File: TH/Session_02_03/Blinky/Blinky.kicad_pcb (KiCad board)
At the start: 2 copper layers, 12 parts, among them U1 TLC551CD‎

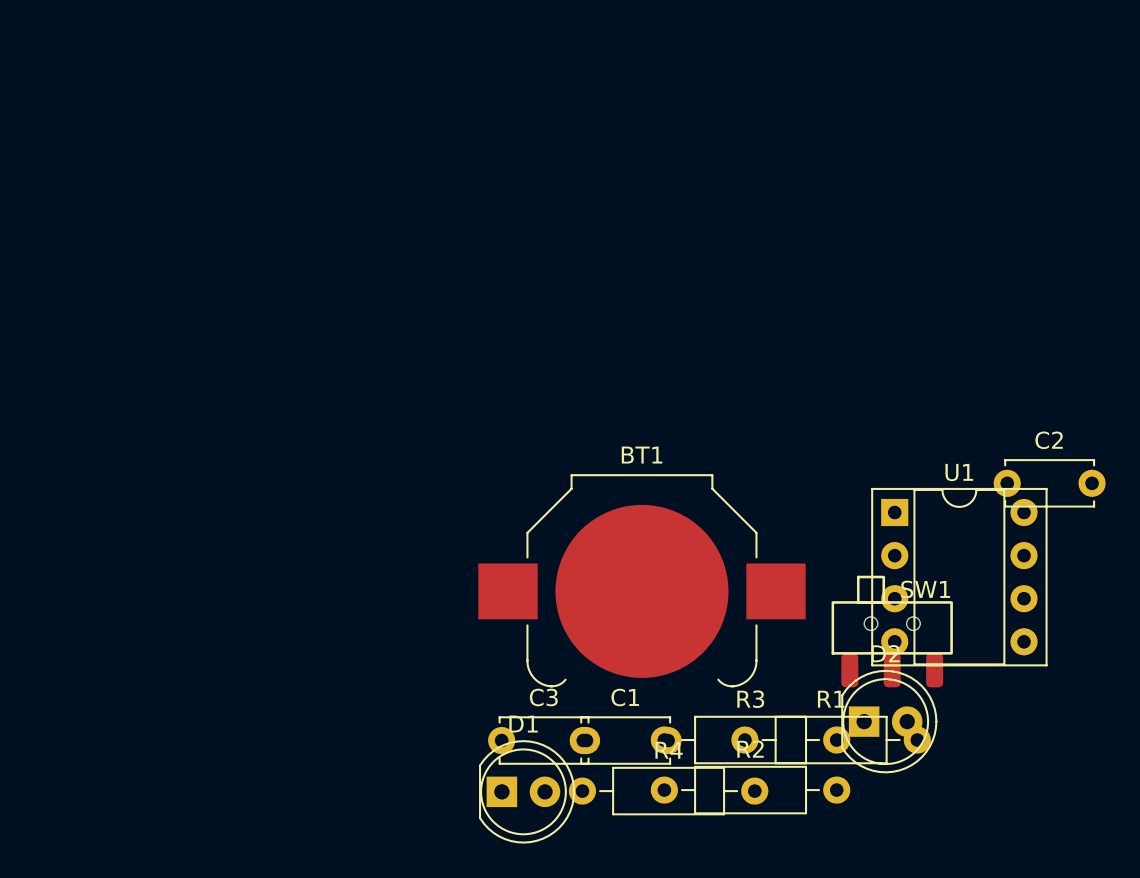
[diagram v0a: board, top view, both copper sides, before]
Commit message: Revamps the through-hole project as transistor based
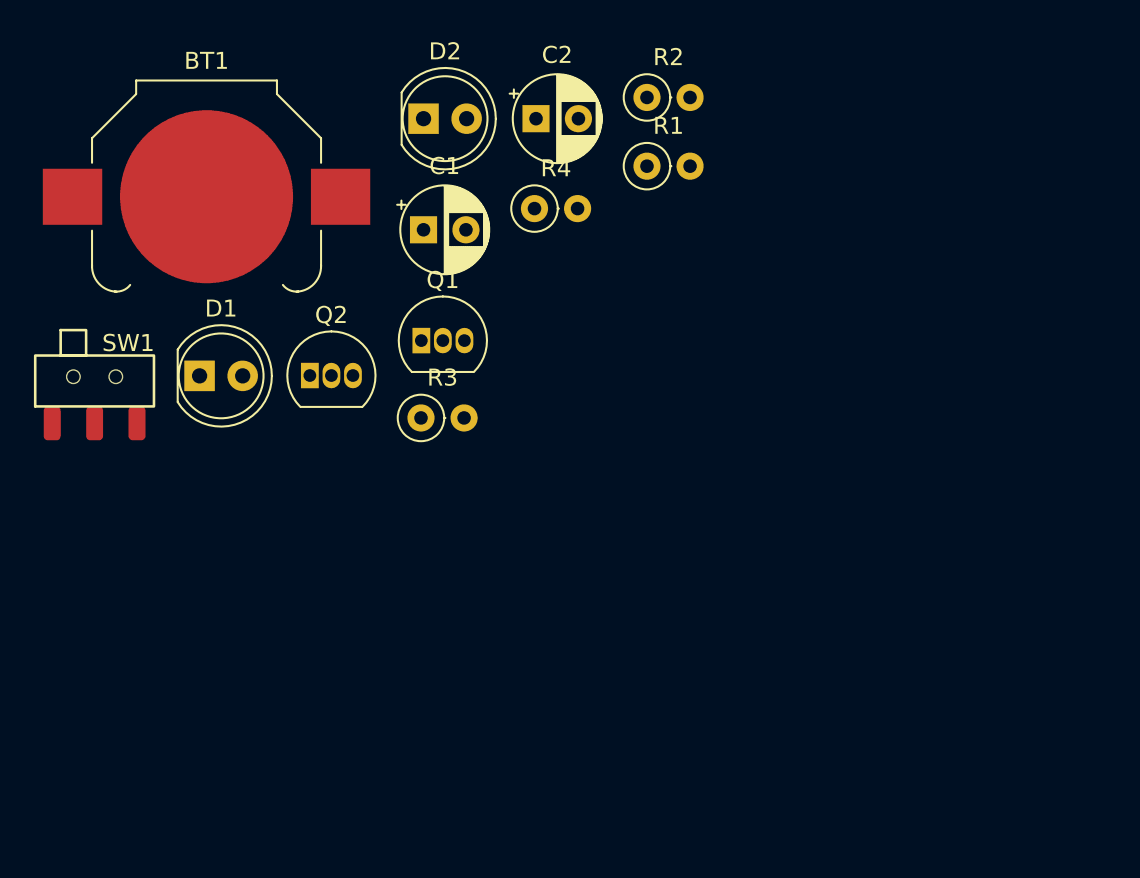
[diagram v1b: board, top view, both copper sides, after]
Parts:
- removed C3: 100nF, Capacitor_THT:C_Disc_D5.0mm_W2.5mm_P5.00mm
- removed SW?: SW_SPDT, Blinky_ZAM:SSK-1202
- removed U1: TLC551CD‎, Package_DIP:DIP-8_W7.62mm_Socket
- added Q1: 2N3904, Package_TO_SOT_THT:TO-92_Inline, F.Cu at (128.8, 81.1)
- added Q2: 2N3904, Package_TO_SOT_THT:TO-92_Inline, F.Cu at (122.2, 83.2)
- added SW1: SW_SPST, Blinky_ZAM:SSK-1202, F.Cu at (109.5, 86.0)
- C1: value 300nF -> 10μF; footprint Capacitor_THT:C_Disc_D5.0mm_W2.5mm_P5.00mm -> Capacitor_THT:CP_Radial_D5.0mm_P2.50mm
- C2: value 100nF -> 10μF; footprint Capacitor_THT:C_Disc_D5.0mm_W2.5mm_P5.00mm -> Capacitor_THT:CP_Radial_D5.0mm_P2.50mm
- R1: value 10kΩ -> 220Ω; footprint Resistor_THT:R_Axial_DIN0207_L6.3mm_D2.5mm_P10.16mm_Horizontal -> Resistor_THT:R_Axial_DIN0207_L6.3mm_D2.5mm_P2.54mm_Vertical
- R2: value 1MΩ -> 100kΩ; footprint Resistor_THT:R_Axial_DIN0207_L6.3mm_D2.5mm_P10.16mm_Horizontal -> Resistor_THT:R_Axial_DIN0207_L6.3mm_D2.5mm_P2.54mm_Vertical
- R3: value 200Ω -> 100kΩ; footprint Resistor_THT:R_Axial_DIN0207_L6.3mm_D2.5mm_P10.16mm_Horizontal -> Resistor_THT:R_Axial_DIN0207_L6.3mm_D2.5mm_P2.54mm_Vertical
- R4: value 200Ω -> 220Ω; footprint Resistor_THT:R_Axial_DIN0207_L6.3mm_D2.5mm_P10.16mm_Horizontal -> Resistor_THT:R_Axial_DIN0207_L6.3mm_D2.5mm_P2.54mm_Vertical
- moved D2 44.0 mm to (128.9, 68.0)
- moved R2 40.8 mm to (142.1, 66.8)
- moved C2 35.1 mm to (135.5, 68.0)
- moved BT1 34.6 mm to (116.1, 72.6)
- moved R4 34.5 mm to (135.4, 73.3)
- moved R1 34.3 mm to (142.1, 70.8)
- moved C1 31.5 mm to (128.9, 74.6)
- moved D1 30.3 mm to (115.7, 83.2)
- moved R3 23.8 mm to (128.8, 85.7)
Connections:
- C1 pad 2: GND -> Net-(C1-Pad2)
- C2 pad 2: GND -> Net-(C2-Pad2)
- D1 pad 1: Net-(D1-Pad1) -> Net-(C1-Pad2)
- D1 pad 2: Net-(C2-Pad1) -> Net-(D1-Pad2)
- D2 pad 1: Net-(D2-Pad1) -> Net-(C2-Pad2)
- R1 pad 1: Net-(C2-Pad1) -> Net-(R1-Pad1)
- R1 pad 2: Net-(R1-Pad2) -> Net-(D1-Pad2)
- R2 pad 1: Net-(R1-Pad2) -> Net-(R1-Pad1)
- R3 pad 1: Net-(D1-Pad1) -> Net-(R1-Pad1)
- R3 pad 2: Net-(D2-Pad2) -> Net-(C2-Pad1)
- R4 pad 1: Net-(D2-Pad1) -> Net-(R1-Pad1)
- R4 pad 2: GND -> Net-(D2-Pad2)

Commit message: Makes corrections to the design rules
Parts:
- added J1: Jumper_1, TestPoint:TestPoint_THTPad_2.0x2.0mm_Drill1.0mm, F.Cu at (137.9, 81.2)
- added J2: Jumper_1, TestPoint:TestPoint_THTPad_2.0x2.0mm_Drill1.0mm, F.Cu at (137.9, 86.3)
- added J4: Jumper_1, TestPoint:TestPoint_THTPad_2.0x2.0mm_Drill1.0mm, F.Cu at (142.9, 86.3)
- added J?: Jumper_1, TestPoint:TestPoint_THTPad_2.0x2.0mm_Drill1.0mm, F.Cu at (142.9, 81.2)
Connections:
- Q1 pad 2: Net-(C2-Pad1) -> Net-(J1-Pad1)
- Q2 pad 2: Net-(C1-Pad1) -> Net-(J4-Pad1)
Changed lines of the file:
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@@
     (48 "B.Fab" user)
     (49 "F.Fab" user)
-    (50 "User.1" user)
-    (51 "User.2" user)
-    (52 "User.3" user)
-    (53 "User.4" user)
-    (54 "User.5" user)
-    (55 "User.6" user)
-    (56 "User.7" user)
-    (57 "User.8" user)
-    (58 "User.9" user)
+    (50 "User.1" user "Nutzer.1")
+    (51 "User.2" user "Nutzer.2")
+    (52 "User.3" user "Nutzer.3")
+    (53 "User.4" user "Nutzer.4")
+    (54 "User.5" user "Nutzer.5")
+    (55 "User.6" user "Nutzer.6")
+    (56 "User.7" user "Nutzer.7")
+    (57 "User.8" user "Nutzer.8")
+    (58 "User.9" user "Nutzer.9")
   )
   (setup
@@
   (net 8 "Net-(D2-Pad2)")
   (net 9 "Net-(R1-Pad1)")
+  (net 10 "Net-(J1-Pad1)")
+  (net 11 "Net-(J4-Pad1)")
   (footprint "Resistor_THT:R_Axial_DIN0207_L6.3mm_D2.5mm_P2.54mm_Vertical" (layer "F.Cu")
     (at 142.07 66.76)
@@
       (net 2 "GND") (pinfunction "E") (pintype "passive"))
     (pad "2" thru_hole oval (at 1.27 0) (size 1.05 1.5) (drill 0.75) (layers *.Cu *.Mask)
-      (net 3 "Net-(C1-Pad1)") (pinfunction "B") (pintype "passive"))
+      (net 11 "Net-(J4-Pad1)") (pinfunction "B") (pintype "passive"))
     (pad "3" thru_hole oval (at 2.54 0) (size 1.05 1.5) (drill 0.75) (layers *.Cu *.Mask)
       (net 6 "Net-(C2-Pad2)") (pinfunction "C") (pintype "passive"))
@@
       (net 2 "GND") (pinfunction "E") (pintype "passive"))
     (pad "2" thru_hole oval (at 1.27 0) (size 1.05 1.5) (drill 0.75) (layers *.Cu *.Mask)
-      (net 5 "Net-(C2-Pad1)") (pinfunction "B") (pintype "passive"))
+      (net 10 "Net-(J1-Pad1)") (pinfunction "B") (pintype "passive"))
     (pad "3" thru_hole oval (at 2.54 0) (size 1.05 1.5) (drill 0.75) (layers *.Cu *.Mask)
       (net 4 "Net-(C1-Pad2)") (pinfunction "C") (pintype "passive"))
@@
       (rotate (xyz 0 0 0))
     )
+  )
+  (footprint "TestPoint:TestPoint_THTPad_2.0x2.0mm_Drill1.0mm" (layer "F.Cu")
+    (at 137.9 86.29)
+    (descr "THT rectangular pad as test Point, square 2.0mm_Drill1.0mm  side length, hole diameter 1.0mm")
+    (tags "test point THT pad rectangle square")
+    (property "Sheetfile" "Blinky.kicad_sch")
+    (property "Sheetname" "")
+    (attr exclude_from_pos_files)
+    (fp_text reference "J2" (at 0 -1.998) (layer "F.SilkS")
+      (effects (font (size 1 1) (thickness 0.15)))
+    )
+    (fp_text value "Jumper_1" (at 0 2.05) (layer "F.Fab")
+      (effects (font (size 1 1) (thickness 0.15)))
+    )
+    (fp_text user "${REFERENCE}" (at 0 -2) (layer "F.Fab")
+      (effects (font (size 1 1) (thickness 0.15)))
+    )
+    (fp_line (start -1.2 -1.2) (end 1.2 -1.2) (layer "F.SilkS") (width 0.12))
+    (fp_line (start 1.2 -1.2) (end 1.2 1.2) (layer "F.SilkS") (width 0.12))
+    (fp_line (start 1.2 1.2) (end -1.2 1.2) (layer "F.SilkS") (width 0.12))
+    (fp_line (start -1.2 1.2) (end -1.2 -1.2) (layer "F.SilkS") (width 0.12))
+    (fp_line (start -1.5 -1.5) (end 1.5 -1.5) (layer "F.CrtYd") (width 0.05))
+    (fp_line (start 1.5 1.5) (end -1.5 1.5) (layer "F.CrtYd") (width 0.05))
+    (fp_line (start -1.5 -1.5) (end -1.5 1.5) (layer "F.CrtYd") (width 0.05))
+    (fp_line (start 1.5 1.5) (end 1.5 -1.5) (layer "F.CrtYd") (width 0.05))
+    (pad "1" thru_hole rect (at 0 0) (size 2 2) (drill 1) (layers *.Cu *.Mask)
+      (net 3 "Net-(C1-Pad1)") (pintype "unspecified"))
+  )
+  (footprint "TestPoint:TestPoint_THTPad_2.0x2.0mm_Drill1.0mm" (layer "F.Cu")
+    (at 142.95 81.24)
+    (descr "THT rectangular pad as test Point, square 2.0mm_Drill1.0mm  side length, hole diameter 1.0mm")
+    (tags "test point THT pad rectangle square")
+    (property "Reference" "J?")
+    (property "Sheetfile" "Blinky.kicad_sch")
+    (property "Sheetname" "")
+    (property "Value" "Jumper_1")
+    (attr exclude_from_pos_files)
+    (fp_text reference "J3" (at 0 -1.998) (layer "F.SilkS")
+      (effects (font (size 1 1) (thickness 0.15)))
+    )
+    (fp_text value "Jumper_1" (at 0 2.05) (layer "F.Fab")
+      (effects (font (size 1 1) (thickness 0.15)))
+    )
+    (fp_text user "${REFERENCE}" (at 0 -2) (layer "F.Fab")
+      (effects (font (size 1 1) (thickness 0.15)))
+    )
+    (fp_line (start 1.2 1.2) (end -1.2 1.2) (layer "F.SilkS") (width 0.12))
+    (fp_line (start -1.2 1.2) (end -1.2 -1.2) (layer "F.SilkS") (width 0.12))
+    (fp_line (start -1.2 -1.2) (end 1.2 -1.2) (layer "F.SilkS") (width 0.12))
+    (fp_line (start 1.2 -1.2) (end 1.2 1.2) (layer "F.SilkS") (width 0.12))
+    (fp_line (start 1.5 1.5) (end 1.5 -1.5) (layer "F.CrtYd") (width 0.05))
+    (fp_line (start -1.5 -1.5) (end -1.5 1.5) (layer "F.CrtYd") (width 0.05))
+    (fp_line (start -1.5 -1.5) (end 1.5 -1.5) (layer "F.CrtYd") (width 0.05))
+    (fp_line (start 1.5 1.5) (end -1.5 1.5) (layer "F.CrtYd") (width 0.05))
+    (pad "1" thru_hole rect (at 0 0) (size 2 2) (drill 1) (layers *.Cu *.Mask)
+      (net 5 "Net-(C2-Pad1)") (pintype "unspecified"))
   )
   (footprint "Capacitor_THT:CP_Radial_D5.0mm_P2.50mm" (layer "F.Cu")
@@
     )
   )
+  (footprint "TestPoint:TestPoint_THTPad_2.0x2.0mm_Drill1.0mm" (layer "F.Cu")
+    (at 137.9 81.24)
+    (descr "THT rectangular pad as test Point, square 2.0mm_Drill1.0mm  side length, hole diameter 1.0mm")
+    (tags "test point THT pad rectangle square")
+    (property "Sheetfile" "Blinky.kicad_sch")
+    (property "Sheetname" "")
+    (attr exclude_from_pos_files)
+    (fp_text reference "J1" (at 0 -1.998) (layer "F.SilkS")
+      (effects (font (size 1 1) (thickness 0.15)))
+    )
+    (fp_text value "Jumper_1" (at 0 2.05) (layer "F.Fab")
+      (effects (font (size 1 1) (thickness 0.15)))
+    )
+    (fp_text user "${REFERENCE}" (at 0 -2) (layer "F.Fab")
+      (effects (font (size 1 1) (thickness 0.15)))
+    )
+    (fp_line (start -1.2 1.2) (end -1.2 -1.2) (layer "F.SilkS") (width 0.12))
+    (fp_line (start 1.2 1.2) (end -1.2 1.2) (layer "F.SilkS") (width 0.12))
+    (fp_line (start 1.2 -1.2) (end 1.2 1.2) (layer "F.SilkS") (width 0.12))
+    (fp_line (start -1.2 -1.2) (end 1.2 -1.2) (layer "F.SilkS") (width 0.12))
+    (fp_line (start -1.5 -1.5) (end -1.5 1.5) (layer "F.CrtYd") (width 0.05))
+    (fp_line (start -1.5 -1.5) (end 1.5 -1.5) (layer "F.CrtYd") (width 0.05))
+    (fp_line (start 1.5 1.5) (end -1.5 1.5) (layer "F.CrtYd") (width 0.05))
+    (fp_line (start 1.5 1.5) (end 1.5 -1.5) (layer "F.CrtYd") (width 0.05))
+    (pad "1" thru_hole rect (at 0 0) (size 2 2) (drill 1) (layers *.Cu *.Mask)
+      (net 10 "Net-(J1-Pad1)") (pintype "unspecified"))
+  )
   (footprint "Resistor_THT:R_Axial_DIN0207_L6.3mm_D2.5mm_P2.54mm_Vertical" (layer "F.Cu")
     (at 142.07 70.81)
@@
     )
   )
+  (footprint "TestPoint:TestPoint_THTPad_2.0x2.0mm_Drill1.0mm" (layer "F.Cu")
+    (at 142.95 86.29)
+    (descr "THT rectangular pad as test Point, square 2.0mm_Drill1.0mm  side length, hole diameter 1.0mm")
+    (tags "test point THT pad rectangle square")
+    (property "Sheetfile" "Blinky.kicad_sch")
+    (property "Sheetname" "")
+    (attr exclude_from_pos_files)
+    (fp_text reference "J4" (at 0 -1.998) (layer "F.SilkS")
+      (effects (font (size 1 1) (thickness 0.15)))
+    )
+    (fp_text value "Jumper_1" (at 0 2.05) (layer "F.Fab")
+      (effects (font (size 1 1) (thickness 0.15)))
+    )
+    (fp_text user "${REFERENCE}" (at 0 -2) (layer "F.Fab")
+      (effects (font (size 1 1) (thickness 0.15)))
+    )
+    (fp_line (start -1.2 1.2) (end -1.2 -1.2) (layer "F.SilkS") (width 0.12))
+    (fp_line (start -1.2 -1.2) (end 1.2 -1.2) (layer "F.SilkS") (width 0.12))
+    (fp_line (start 1.2 -1.2) (end 1.2 1.2) (layer "F.SilkS") (width 0.12))
+    (fp_line (start 1.2 1.2) (end -1.2 1.2) (layer "F.SilkS") (width 0.12))
+    (fp_line (start -1.5 -1.5) (end -1.5 1.5) (layer "F.CrtYd") (width 0.05))
+    (fp_line (start -1.5 -1.5) (end 1.5 -1.5) (layer "F.CrtYd") (width 0.05))
+    (fp_line (start 1.5 1.5) (end -1.5 1.5) (layer "F.CrtYd") (width 0.05))
+    (fp_line (start 1.5 1.5) (end 1.5 -1.5) (layer "F.CrtYd") (width 0.05))
+    (pad "1" thru_hole rect (at 0 0) (size 2 2) (drill 1) (layers *.Cu *.Mask)
+      (net 11 "Net-(J4-Pad1)") (pintype "unspecified"))
+  )
   (footprint "LED_THT:LED_D5.0mm" (layer "F.Cu")

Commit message: Corrections to the switch footprint
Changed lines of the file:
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@@
       (effects (font (size 1 1) (thickness 0.15)))
     )
-    (fp_rect (start -3.500001 -1) (end 3.500001 -4) (layer "F.SilkS") (width 0.1524) (fill none))
     (fp_rect (start -2 -5.499999) (end -0.5 -4) (layer "F.SilkS") (width 0.1524) (fill none))
+    (fp_rect (start -3.500001 -1.1) (end 3.500001 -4) (layer "F.SilkS") (width 0.1524) (fill none))
     (fp_rect (start -3.5 -5.5) (end 3.5 1) (layer "F.CrtYd") (width 0.01) (fill none))
-    (pad "" np_thru_hole circle (at -1.25 -2.75) (size 0.8 0.8) (drill 0.8) (layers F&B.Cu *.Mask))
-    (pad "" np_thru_hole circle (at 1.25 -2.75) (size 0.8 0.8) (drill 0.8) (layers F&B.Cu *.Mask))
+    (pad "" np_thru_hole circle (at -1.5 -2.75) (size 0.8 0.8) (drill 0.8) (layers F&B.Cu *.Mask))
+    (pad "" np_thru_hole circle (at 1.5 -2.75) (size 0.8 0.8) (drill 0.8) (layers F&B.Cu *.Mask))
     (pad "1" smd roundrect (at -2.5 0) (size 1 2) (layers "F.Cu" "F.Paste" "F.Mask") (roundrect_rratio 0.25)
       (net 1 "Net-(BT1-Pad1)") (pinfunction "A") (pintype "passive"))
